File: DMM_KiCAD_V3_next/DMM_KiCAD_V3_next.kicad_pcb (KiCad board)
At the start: 4 copper layers, 68.5 x 53.2 mm, 68 parts, among them J1 Conn_01x07_Pin, J10 ANALOG, J11 I_Input, J12 Conn_01x02_Pin, J13 DIGITAL1, J14 Barrel_Jack, J15 Barrel_Jack, J2 MicoSD, J3 Conn_01x07_Pin, J31 Conn_01x04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

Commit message: Working on a Giga-COmpatible DMM code.
Also working on adding level shifting to the next PCB design.
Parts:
- removed TP3: Batt Input, Connector_PinHeader_2.54mm:PinHeader_1x01_P2.54mm_Vertical
- added J7: Conn_01x02_Pin, Connector_PinSocket_2.54mm:PinSocket_1x02_P2.54mm_Vertical, F.Cu at (83.2, 53.3)
- added Q6: BSS138, Package_TO_SOT_SMD:SOT-23, F.Cu at (70.8, 76.8)
- added Q7: BSS138, Package_TO_SOT_SMD:SOT-23, F.Cu at (70.8, 81.9)
- added R10: 10K, Resistor_SMD:R_0805_2012Metric_Pad1.20x1.40mm_HandSolder, F.Cu at (74.3, 77.7)
- added R11: 10K, Resistor_SMD:R_0805_2012Metric_Pad1.20x1.40mm_HandSolder, F.Cu at (67.3, 76.8)
- added R19: 10K, Resistor_SMD:R_0805_2012Metric_Pad1.20x1.40mm_HandSolder, F.Cu at (67.3, 81.9)
- added R20: 10K, Resistor_SMD:R_0805_2012Metric_Pad1.20x1.40mm_HandSolder, F.Cu at (74.3, 81.9)
- F1: footprint Fuse:Fuseholder_Clip-5x20mm_Keystone_3512P_Inline_P23.62x7.27mm_D1.02x2.41x1.02x1.57mm_Horizontal -> Fuse:Fuse_1206_3216Metric_Pad1.42x1.75mm_HandSolder
- moved F1 13.0 mm to (139.7, 75.6)
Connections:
- J9 pad 1: SDA -> SDA-5V
- J9 pad 2: SCL -> SCL-5V
- R13 pad 1: SCL -> SCL-5V
- R15 pad 1: SDA -> SDA-5V
- U3 pad 10: SCL -> SCL-5V
- U3 pad 9: SDA -> SDA-5V
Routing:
- net SDA: track 102.4 -> 58.0 mm
- net SCL: track 92.8 -> 54.2 mm
- net SDA-5V: track 0.00 -> 23.0 mm
- net SCL-5V: track 0.00 -> 22.1 mm
- net +BATT: track 88.5 -> 98.2 mm
- net Net-(F1-Pad1): track 29.0 -> 22.2 mm, vias 0 -> 1
- net +3V3: track 41.7 -> 46.9 mm
- net VDD: track 158.9 -> 161.1 mm
- net GND: track 61.4 -> 62.1 mm, vias 11 -> 12

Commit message: More updates to the next PCB
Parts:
- moved R10 48.1 mm to (122.4, 76.3)
- moved Q7 48.1 mm to (118.9, 80.6)
- moved R19 48.1 mm to (115.4, 80.6)
- moved R20 48.1 mm to (122.4, 80.6)
- moved Q6 48.1 mm to (118.9, 76.2)
- moved R11 48.1 mm to (115.4, 76.2)
- moved F1 13.7 mm to (127.0, 80.6), turned to -90 degrees
- moved U11 12.5 mm to (110.2, 75.9), turned to -90 degrees
- moved R6 6.12 mm to (123.2, 72.4), turned to 180 degrees
- moved J7 0.61 mm to (83.8, 53.3)
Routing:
- net +3V3: track 46.9 -> 65.8 mm, vias 1 -> 2
- net SDA-5V: track 23.0 -> 40.9 mm, vias 0 -> 2
- net SCL: track 54.2 -> 67.5 mm, vias 1 -> 3
- net SCL-5V: track 22.1 -> 33.2 mm, vias 0 -> 2
- net SDA: track 58.0 -> 69.0 mm, vias 1 -> 3
- net VDD: track 161.1 -> 165.2 mm, vias 8 -> 9
- net /R Circuit I Output: track 19.8 -> 22.3 mm
- net MISO: track 42.3 -> 44.8 mm
- net GND: track 62.1 -> 60.1 mm
- net CLK: track 42.0 -> 43.1 mm
- net D3~: track 87.6 -> 86.7 mm

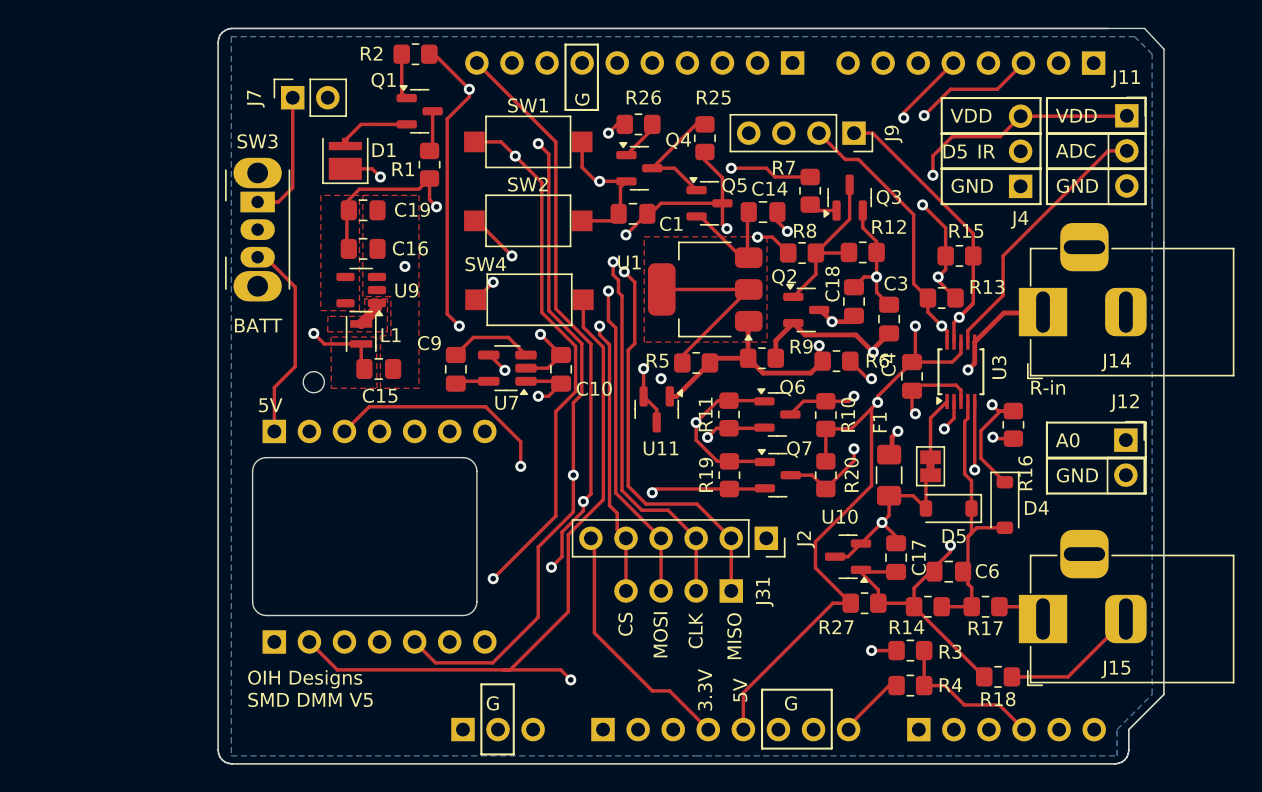
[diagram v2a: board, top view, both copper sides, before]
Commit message: PCB updates.
 Added the option for four-wire resistance measurements
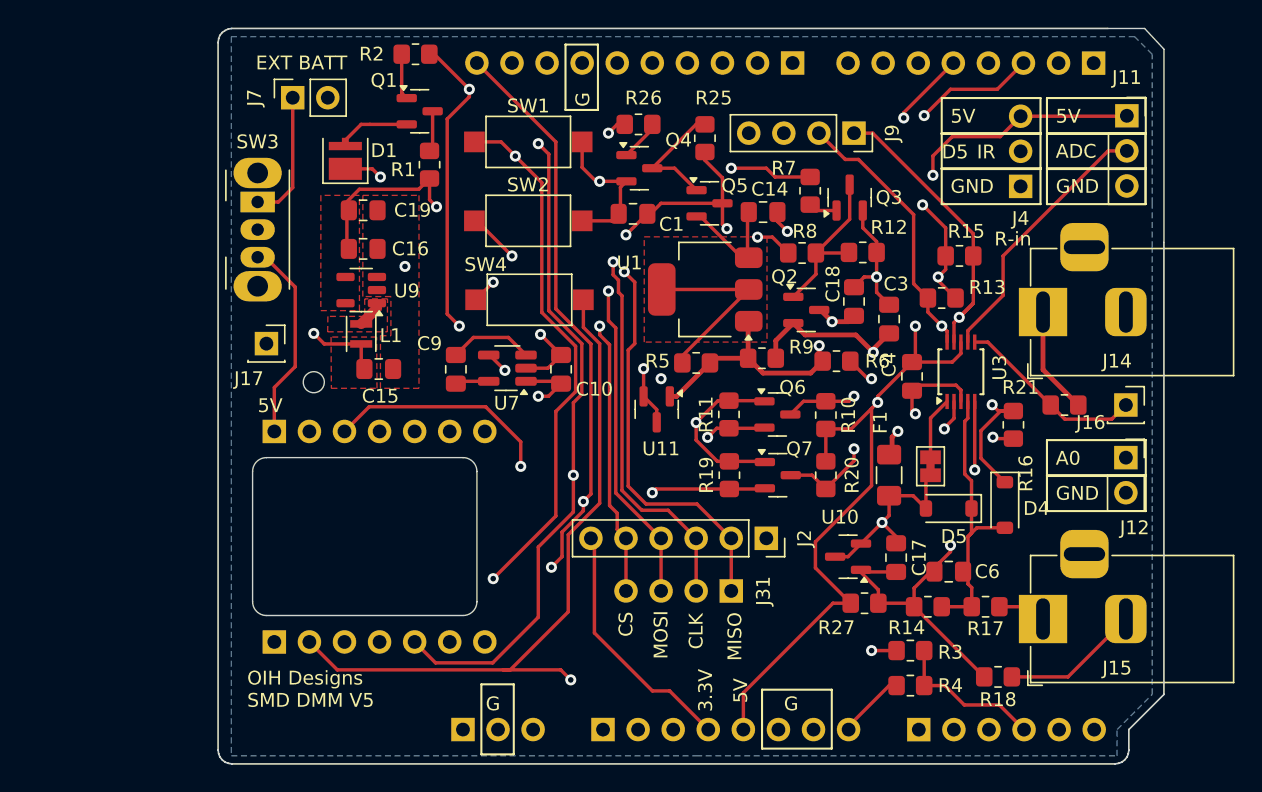
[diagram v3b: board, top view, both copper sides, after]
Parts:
- added J16: Conn_01x01_Socket, Connector_PinSocket_2.54mm:PinSocket_1x01_P2.54mm_Vertical, F.Cu at (144.1, 75.6)
- added J17: Conn_01x01_Socket, Connector_PinSocket_2.54mm:PinSocket_1x01_P2.54mm_Vertical, F.Cu at (81.9, 71.1)
- added R21: 0, Resistor_SMD:R_0805_2012Metric_Pad1.20x1.40mm_HandSolder, F.Cu at (139.7, 75.6)
- moved J12 1.27 mm to (144.1, 79.4)
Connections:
- U3 pad 6: Resistor_Input -> /R into ADS
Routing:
- net /R into ADS: track 0.00 -> 13.7 mm
- net Resistor_Input: track 27.5 -> 34.4 mm, vias 2 -> 1
- net XIAO Batt Pin: track 15.8 -> 19.5 mm
- net A0/D14: track 76.5 -> 75.9 mm
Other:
- board text added: "EXT BATT"
- board text removed: "BATT"
- board text removed: "VDD"

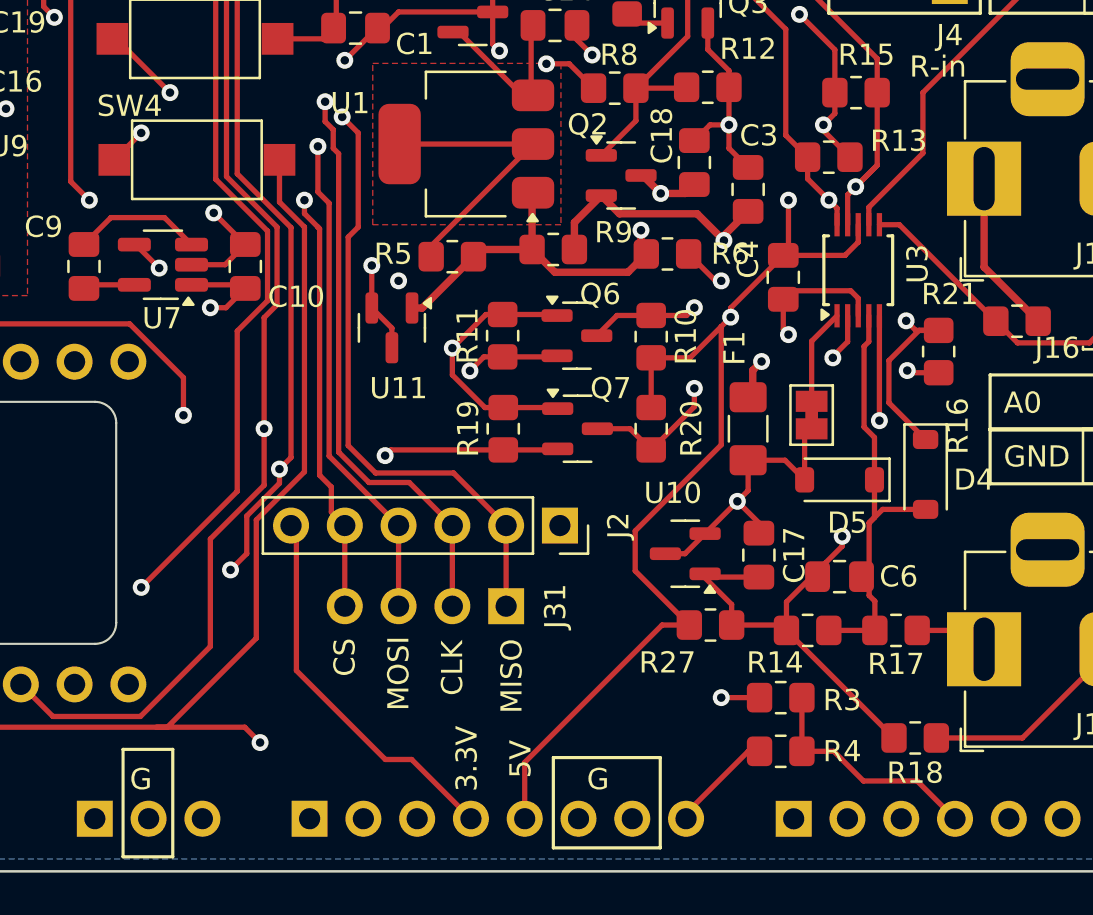
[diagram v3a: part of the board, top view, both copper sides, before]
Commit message: Added Touchscreen Buttons to the Giga Shield Version
Revised next PCB for power input options
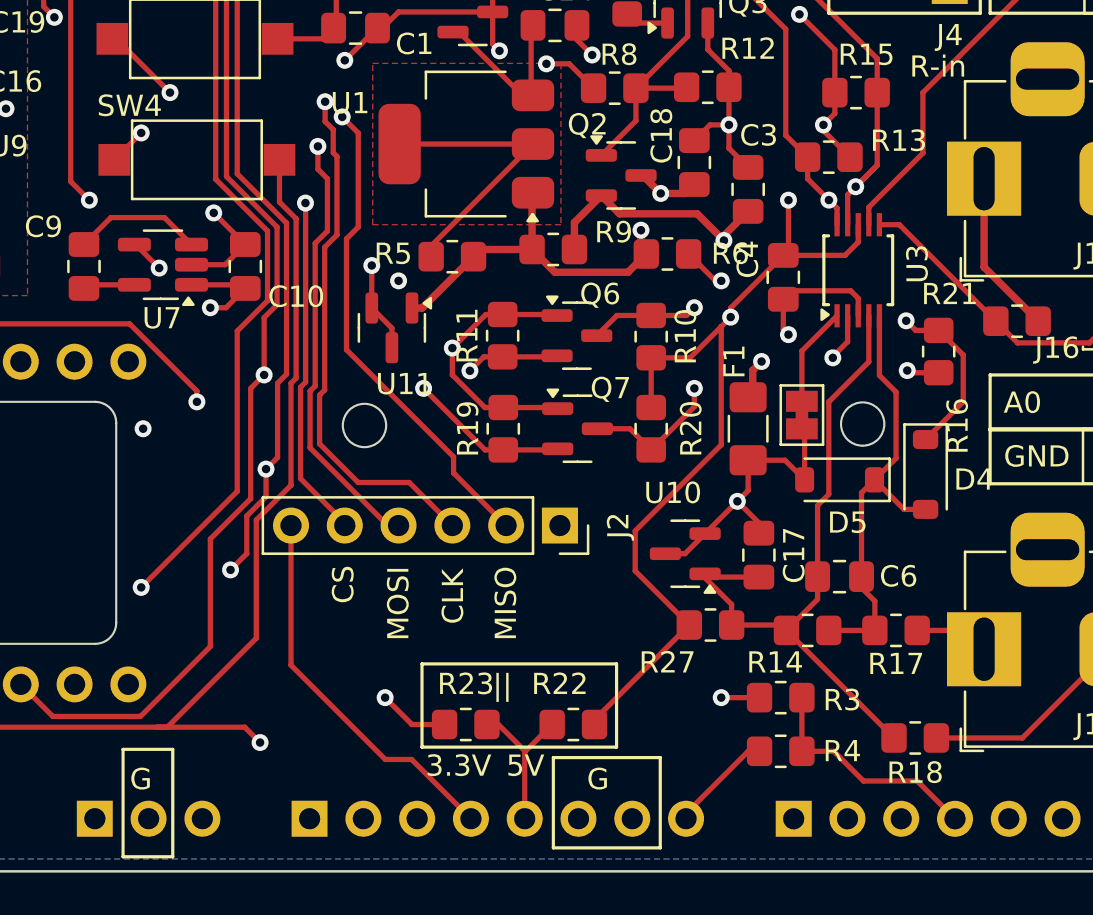
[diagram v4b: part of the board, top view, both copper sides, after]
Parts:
- removed J31: Conn_01x04, Connector_PinHeader_2.54mm:PinHeader_1x04_P2.54mm_Vertical
- added R22: 0, Resistor_SMD:R_0805_2012Metric_Pad1.20x1.40mm_HandSolder, F.Cu at (118.7, 94.6)
- added R23: 0, Resistor_SMD:R_0805_2012Metric_Pad1.20x1.40mm_HandSolder, F.Cu at (113.7, 94.6)
- moved JP6 0.46 mm to (129.5, 80.0)
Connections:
- J6 pad 5: VDD -> /Uno5vPin
- J6 pad 8: +BATT -> +VSW
- R4 pad 2: +BATT -> +VSW
- U3 pad 4: /V Signal to ADS -> /V Ref to ADS
- U3 pad 5: /V Ref to ADS -> /V Signal to ADS
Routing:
- net +BATT: track 98.2 -> 57.8 mm, vias 0 -> 2
- net VDD: track 165.2 -> 157.6 mm
- net /Uno5vPin: track 0.00 -> 7.32 mm
- net MISO: track 44.8 -> 38.9 mm
- net +VSW: track 0.00 -> 4.94 mm
- net CS: track 43.3 -> 39.6 mm
- net CLK: track 43.1 -> 40.2 mm
- net MOSI: track 42.6 -> 39.8 mm
- net +3V3: track 65.8 -> 67.4 mm
- net SDA: track 69.0 -> 69.8 mm
- net /V Signal to ADS: track 20.5 -> 21.3 mm
- net /V Ref to ADS: track 32.0 -> 31.8 mm, vias 2 -> 0
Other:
- outline, holes or cut-outs redrawn
- board text added: "||"

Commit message: Further Giga Refinements
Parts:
- moved D5 1.40 mm to (131.3, 84.5)
- moved D4 1.14 mm to (136.5, 82.8)
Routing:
- net GND: track 60.1 -> 59.0 mm
- net /V Signal to ADS: track 21.3 -> 22.4 mm
